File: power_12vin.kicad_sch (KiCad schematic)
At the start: 12 parts, among them U5 TVS1800DRV, U6 TPS259480AYWPR

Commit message: edit README.md
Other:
- company: (none) -> NOIRLab
- title: (none) -> 4 channel ADC Module
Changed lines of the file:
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@@
 	(generator_version "9.0")
 	(paper "A4")
+	(title_block
+		(title "4 channel ADC Module")
+		(date "2025-04-18")
+		(rev "0.1")
+		(company "NOIRLab")
+		(comment 1 "Design: Braulio Cancino Vera - braulio.cancino@noirlab.edu")
+	)
 	(text "Soft Start Charge Time 15.64 ms\nCurrent Limit Ilim 4.6 A\nBlanking Interval 2.09 ms"
 		(exclude_from_sim no)

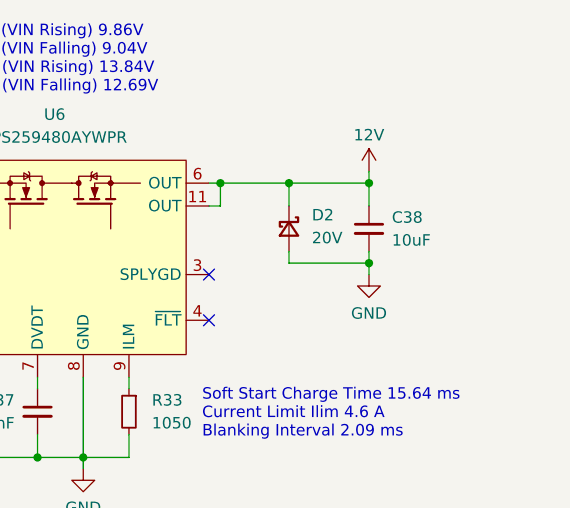
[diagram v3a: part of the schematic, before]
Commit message: Fix BOM.csv
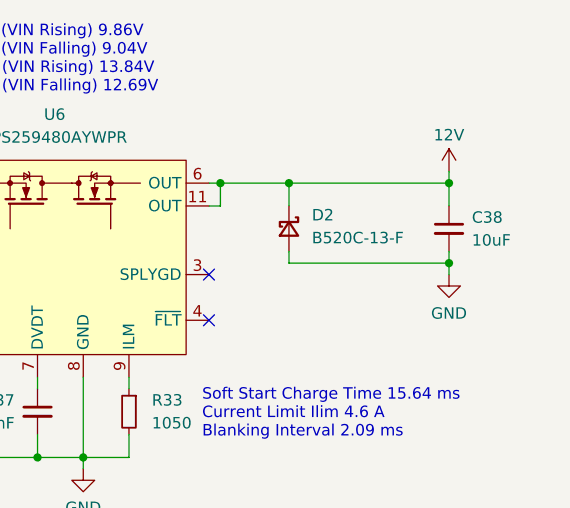
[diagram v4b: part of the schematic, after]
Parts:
- D2: value 20V -> B520C-13-F
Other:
- moved on the sheet: C38
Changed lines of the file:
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@@
-	)
-	(junction
-		(at 193.04 82.55)
-		(diameter 0)
-		(color 0 0 0 0)
 	)
 	(junction
@@
 	)
 	(junction
+		(at 201.93 82.55)
+		(diameter 0)
+		(color 0 0 0 0)
+	)
+	(junction
 		(at 139.7 82.55)
 		(diameter 0)
@@
 	)
 	(junction
-		(at 193.04 91.44)
+		(at 201.93 91.44)
 		(diameter 0)
 		(color 0 0 0 0)
@@
 	(wire
 		(pts
-			(xy 184.15 82.55) (xy 193.04 82.55)
+			(xy 184.15 82.55) (xy 201.93 82.55)
 		)
 		(stroke
@@
 	(wire
 		(pts
-			(xy 193.04 81.28) (xy 193.04 82.55)
+			(xy 201.93 81.28) (xy 201.93 82.55)
 		)
 		(stroke
@@
 	(wire
 		(pts
-			(xy 193.04 85.09) (xy 193.04 82.55)
+			(xy 201.93 85.09) (xy 201.93 82.55)
 		)
 		(stroke
@@
 	(wire
 		(pts
-			(xy 184.15 91.44) (xy 193.04 91.44)
+			(xy 184.15 91.44) (xy 201.93 91.44)
 		)
 		(stroke
@@
 	(wire
 		(pts
-			(xy 193.04 91.44) (xy 193.04 92.71)
+			(xy 201.93 91.44) (xy 201.93 92.71)
 		)
 		(stroke
@@
 	(wire
 		(pts
-			(xy 193.04 90.17) (xy 193.04 91.44)
+			(xy 201.93 90.17) (xy 201.93 91.44)
 		)
 		(stroke
@@
 	(symbol
 		(lib_id "power:+12V")
-		(at 193.04 81.28 0)
+		(at 201.93 81.28 0)
 		(unit 1)
 		(exclude_from_sim no)
@@
 		(dnp no)
 		(property "Reference" "#PWR069"
-			(at 193.04 85.09 0)
+			(at 201.93 85.09 0)
 			(effects
 				(font
@@
 		)
 		(property "Value" "12V"
-			(at 193.04 77.216 0)
+			(at 201.93 77.216 0)
 			(effects
 				(font
@@
 		)
 		(property "Footprint" ""
-			(at 193.04 81.28 0)
+			(at 201.93 81.28 0)
 			(effects
 				(font
@@
 		)
 		(property "Datasheet" ""
-			(at 193.04 81.28 0)
+			(at 201.93 81.28 0)
 			(effects
 				(font
@@
 		)
 		(property "Description" "Power symbol creates a global label with name \"+12V\""
-			(at 193.04 81.28 0)
+			(at 201.93 81.28 0)
 			(effects
 				(font
@@
 		(on_board yes)
 		(dnp no)
-		(fields_autoplaced yes)
 		(property "Reference" "D2"
 			(at 186.69 86.1059 90)
@@
 			)
 		)
-		(property "Value" "20V"
+		(property "Value" "B520C-13-F"
 			(at 186.69 88.6459 90)
 			(effects
@@
 	(symbol
 		(lib_id "Device:C_Small")
-		(at 193.04 87.63 0)
+		(at 201.93 87.63 0)
 		(unit 1)
 		(exclude_from_sim no)
@@
 		(dnp no)
 		(property "Reference" "C38"
-			(at 195.58 86.3662 0)
+			(at 204.47 86.3662 0)
 			(effects
 				(font
@@
 		)
 		(property "Value" "10uF"
-			(at 195.58 88.9062 0)
+			(at 204.47 88.9062 0)
 			(effects
 				(font
@@
 		)
 		(property "Footprint" "Capacitor_SMD:C_1206_3216Metric"
-			(at 193.04 87.63 0)
+			(at 201.93 87.63 0)
 			(effects
 				(font
@@
 		)
 		(property "Datasheet" "~"
-			(at 193.04 87.63 0)
+			(at 201.93 87.63 0)
 			(effects
 				(font
@@
 		)
 		(property "Description" "10 µF ±10% 35V Ceramic Capacitor X7R 1206 (3216 Metric)"
-			(at 193.04 87.63 0)
+			(at 201.93 87.63 0)
 			(effects
 				(font
@@
 		)
 		(property "M" "TAIYO"
-			(at 193.04 87.63 0)
+			(at 201.93 87.63 0)
 			(effects
 				(font
@@
 		)
 		(property "MPN" "GMK316AB7106KL-TR"
-			(at 193.04 87.63 0)
+			(at 201.93 87.63 0)
 			(effects
 				(font
@@
 	(symbol
 		(lib_id "power:GND")
-		(at 193.04 92.71 0)
+		(at 201.93 92.71 0)
 		(unit 1)
 		(exclude_from_sim no)
@@
 		(dnp no)
 		(property "Reference" "#PWR070"
-			(at 193.04 99.06 0)
+			(at 201.93 99.06 0)
 			(effects
 				(font
@@
 		)
 		(property "Value" "GND"
-			(at 193.04 97.028 0)
+			(at 201.93 97.028 0)
 			(effects
 				(font
@@
 		)
 		(property "Footprint" ""
-			(at 193.04 92.71 0)
+			(at 201.93 92.71 0)
 			(effects
 				(font
@@
 		)
 		(property "Datasheet" ""
-			(at 193.04 92.71 0)
+			(at 201.93 92.71 0)
 			(effects
 				(font
@@
 		)
 		(property "Description" "Power symbol creates a global label with name \"GND\" , ground"
-			(at 193.04 92.71 0)
-			(effects
-				(font
+			(at 201.93 92.71 0)
+			(effects
+				(font
